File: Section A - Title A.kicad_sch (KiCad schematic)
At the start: 50 parts, among them J10 Conn_01x26, J11 L17HTHES4R1C, J12 DA15_Socket_MountingHoles, J13 FCR7350R, J14 FCR7350B, J15 DE09-SL-24, J25 KLDX-0202-A-LT, Q3 IRLZ44N, SW1 SW_Rotary_1x9_MP, T1 TestPoint, T10 TestPoint, T2 TestPoint, T3 TestPoint, T4 TestPoint, T5 TestPoint, T6 TestPoint, T9 TestPoint

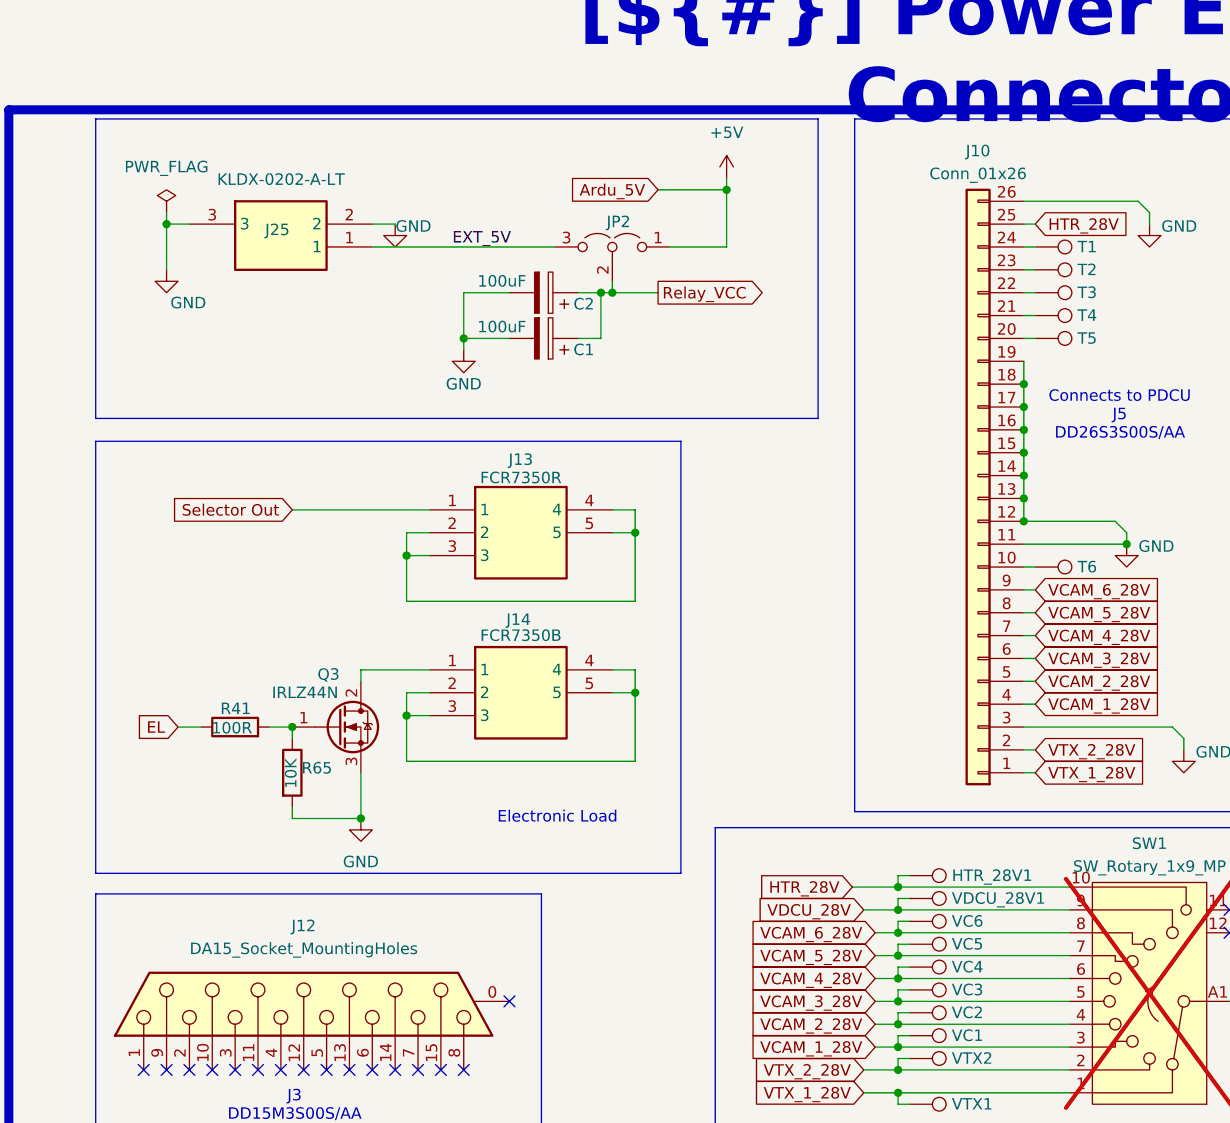
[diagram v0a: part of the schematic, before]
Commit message: created for the Realtra part number
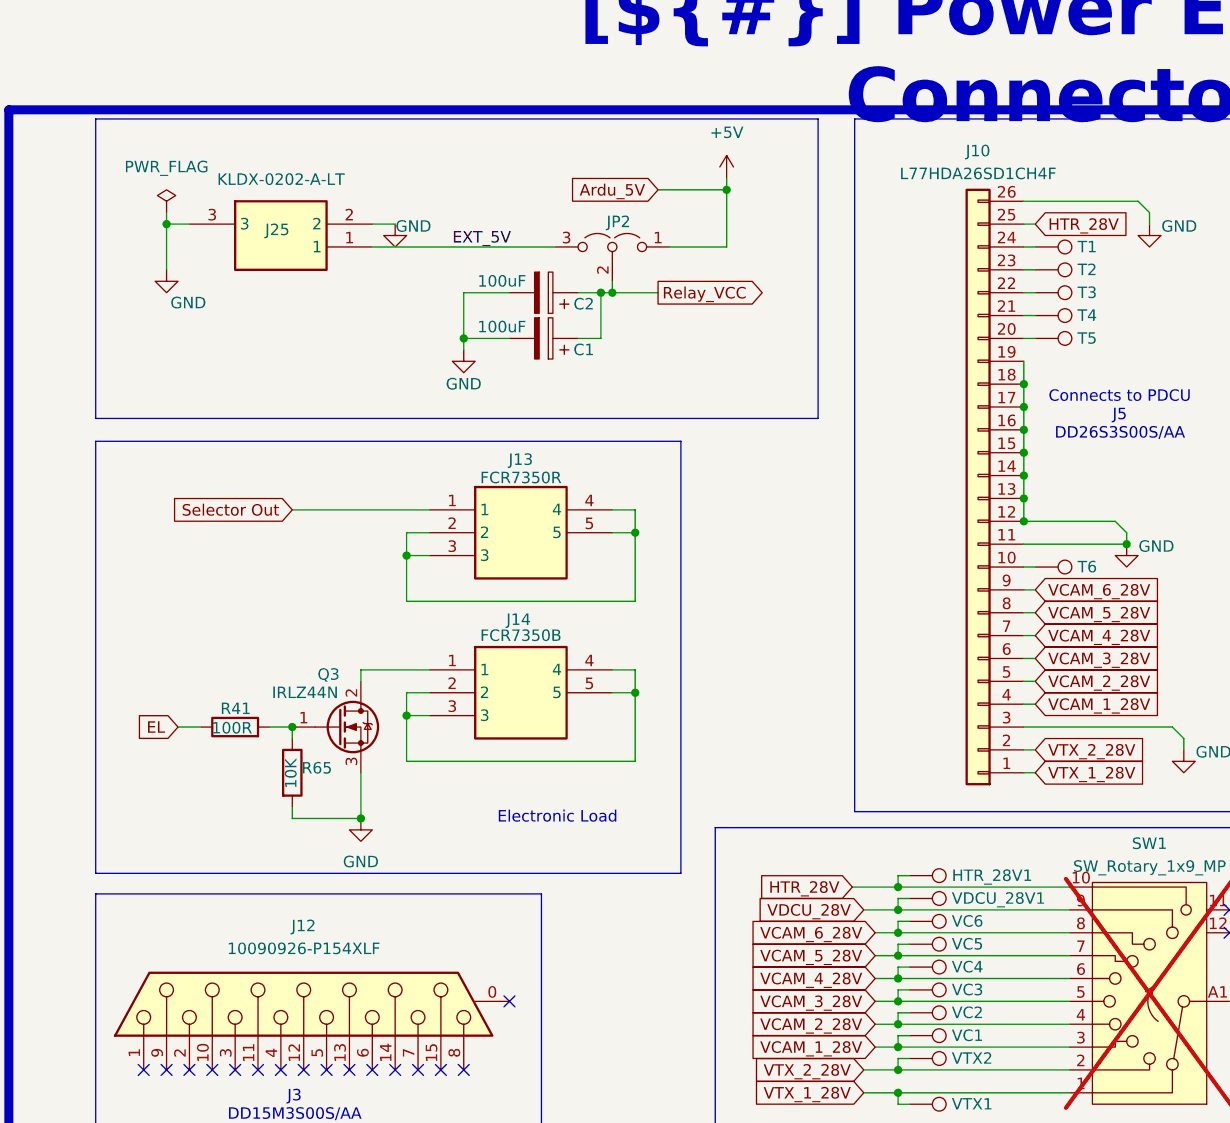
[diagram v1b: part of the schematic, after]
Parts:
- J10: value Conn_01x26 -> L77HDA26SD1CH4F
- J12: value DA15_Socket_MountingHoles -> 10090926-P154XLF
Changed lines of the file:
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@@
 			)
 		)
-		(property "Value" "DA15_Socket_MountingHoles"
+		(property "Value" "10090926-P154XLF"
 			(at 62.23 121.158 90)
 			(effects
@@
 			)
 		)
-		(property "Value" "Conn_01x26"
+		(property "Value" "L77HDA26SD1CH4F"
 			(at 137.16 35.052 0)
 			(effects
